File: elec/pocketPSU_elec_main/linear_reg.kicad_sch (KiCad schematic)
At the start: 0 parts

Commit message: ldo circuit + simulation
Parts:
- added C20, C21: 1u, symbol Device:C_Small
- added C22, C23: 1n, symbol Device:C_Small
- added C24: 100p, symbol Device:C_Small
- added D1: BAV16W, Diode_SMD:D_SOD-123, symbol Diode:BAV16W
- added Q1: SUD08P06-155L, Package_TO_SOT_SMD:TO-252-2, symbol Transistor_FET:SUD08P06-155L
- added R17: 9k, symbol Device:R_US
- added R19, R23: 1k, symbol Device:R_US
- added R20: 0.1, symbol Device:R_US
- added R21: 100, symbol Device:R_US
- added R22, R24: 10k, symbol Device:R_US
- added R25, R26, R27: 100k, symbol Device:R_US
- added R28: 5k, symbol Device:R_US
- added S1: SWITCH, symbol Simulation_SPICE:SWITCH
- added U7: LM358, symbol Amplifier_Operational:LM358
- added V1: 33, symbol Simulation_SPICE:VDC
- added V2: VSIN, symbol Simulation_SPICE:VSIN
- added V3, V4: VPULSE, symbol Simulation_SPICE:VPULSE
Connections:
- new net: C22.1, R21.1
- new net: D1.1 (K), R28.1
- new net: C23.1, R21.2, R23.1, U7.2 (-)
- new net: S1.3 (C+), V3.1
- new net: R17.1, R19.2, R28.2, U7.3 (+)
- new net: C24.2, R22.2, R27.1, U7.6 (-)
- new net: R24.2, R26.1, U7.5 (+)
- new net: Q1.2 (D), R20.2, R24.1
- new net CC_OUT: C24.1, D1.2 (A), U7.7
- new net CV_OUT: C22.2, Q1.1 (G), U7.1
- new net GND: C20.2, C21.2, C23.2, R19.1, R25.1, R26.2, S1.2 (N-), S1.4 (C-), U7.4 (V-), V1.2, V2.2, V3.2, V4.2
- new net Iset: R27.2, V4.1
- new net Vin: C21.1, Q1.3 (S), U7.8 (V+), V1.1
- new net Vout: C20.1, R17.2, R20.1, R22.1, R25.2, S1.1 (N+)
- new net Vset: R23.2, V2.1
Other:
- note added: ".options chgtol=1e-11 abstol=10u"

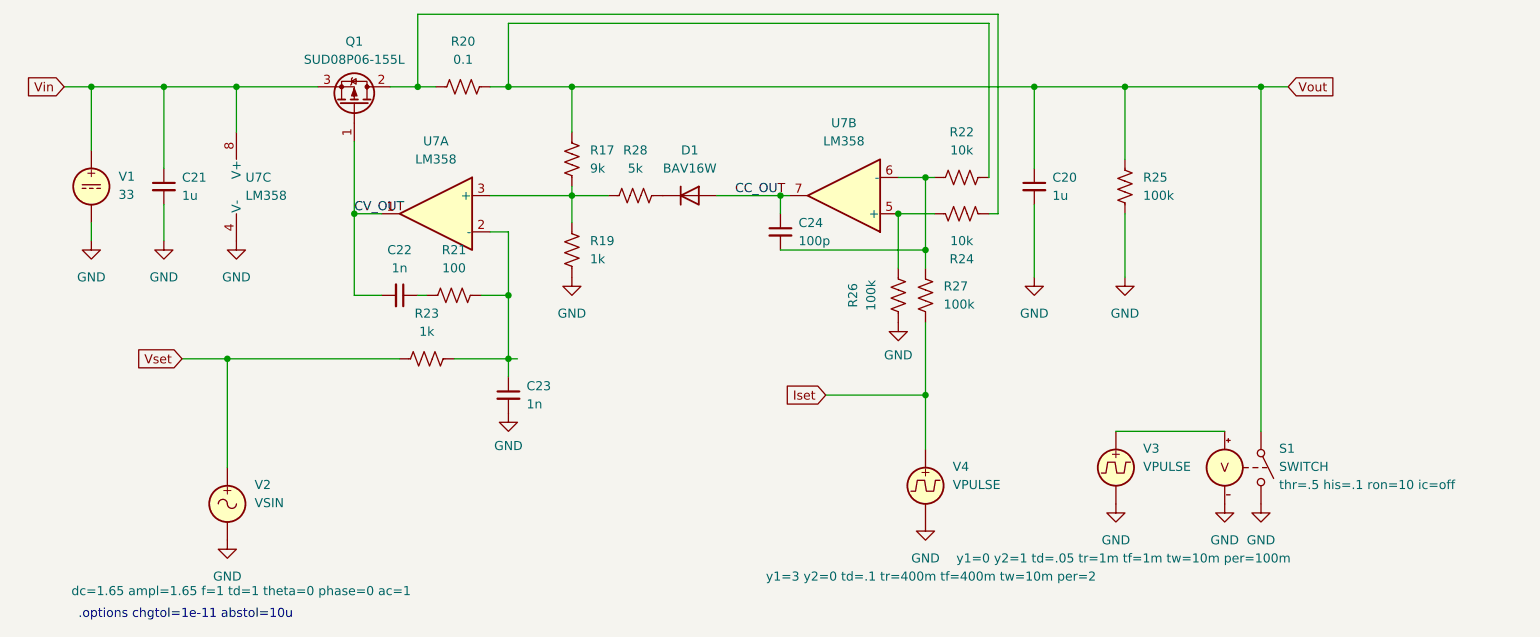
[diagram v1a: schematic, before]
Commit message: tuning for better response
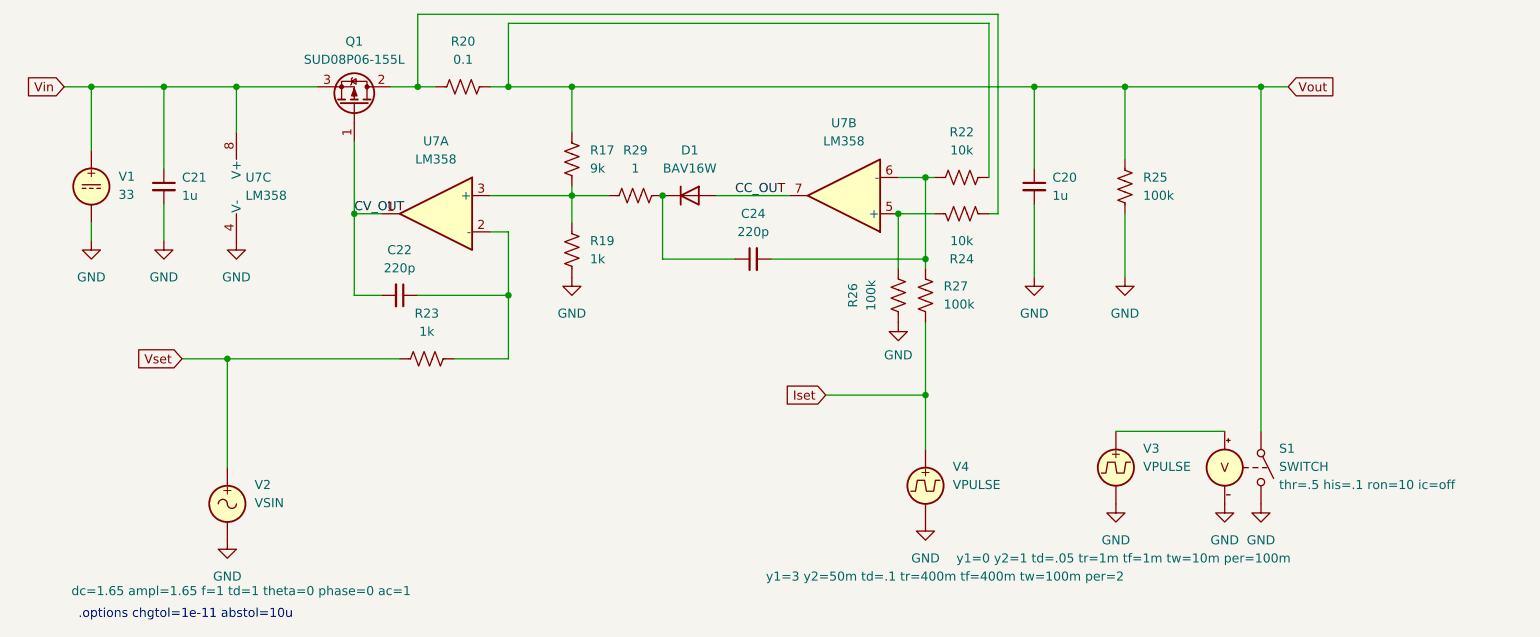
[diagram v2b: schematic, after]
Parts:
- removed C23: 1n, symbol Device:C_Small
- removed R21: 100, symbol Device:R_US
- removed R28: 5k, symbol Device:R_US
- added R29: 1, symbol Device:R_US
- C22: value 1n -> 220p
- C24: value 100p -> 220p
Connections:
- net CC_OUT: no longer C24.1
- net at C22.1: now also R23.1, U7.2 (-)
- net at D1.1 (K): now also C24.1, R29.1
- net at R17.1, R19.2, U7.3 (+): now also R29.2
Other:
- moved on the sheet: C24
